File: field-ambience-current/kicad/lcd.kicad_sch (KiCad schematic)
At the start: 5 parts, among them J3 LCD 1.9in ST7789 320x170 SPI-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, Q2 2N7002 (LCD-Backlight Low-Sid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

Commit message: audit: fix J3/J6/J7 LCSC doc-drift; flag H743 firmware cell-read gap (r18.76)
User asked to check for any BOM or device-functionality issues. Ran a
systematic audit:

BOM checks:
- No duplicate reference designators across all 201 placed instances
  (verified against the schematic's actual instance paths, not the
  per-sheet symbol-library templates which share generic single-letter
  placeholder refs by design).
- jlc_bom.csv parses cleanly despite several part descriptions containing
  embedded commas (properly CSV-quoted).
- Generator output verified deterministic across repeated runs.

Found and fixed a real doc<->generator drift: the generator had placeholder
"TBD" text in the LCSC field for J3 (LCD module header) and J6/J7 (speaker
headers), even though BOM_MASTER.md already documented the real, correct
codes for these on-board pin headers (C124383 for J3, C124375 for J6/J7) --
the docs had been updated at some point but the generator itself never was.
Synced the generator to use the already-verified codes; jlc_bom.csv now has
zero remaining placeholder LCSC values except the one legitimate case (J4
Tag-Connect, a genuine vendor-direct part with no LCSC listing, already
audited in BOM_MASTER's r18.37 entry).

Functionality check (found, NOT fixed -- flagging only, this session stays
hardware-only per prior PRs):
- src/hal_h743/main_h743.c (the actual STM32H743 product target) still has
  a commented-out TODO stub describing the retired analog Hall-ADC cell-read
  path (adc_read_norm), which has had no signal source since r18.73 moved
  cells to digital MCP23017 GPIO buttons. If implemented literally as
  written, cells would not function on real hardware.
- src/hal_pico/main_pico.c (the bench target) already has a correct, tested
  implementation: it reads cell presses as MCP23017 GPIO edges directly
  (mirroring the modifier-button code two lines above it in the same main
  loop) and calls engine_note_on/off, bypassing the old velocity state
  machine entirel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
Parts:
- J3: LCSC TBD (Modul, separat bestellen) -> C124383; MPN TBD (LCD-Modul separat: Adafruit 5394-Klasse / ER-TFT019) -> 1x8 2.54mm pin header (the on-board connector; the LCD modu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
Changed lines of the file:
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@@
       (property "Datasheet" "~" (at 140.0 100.0 0)
         (effects (font (size 1.27 1.27)) hide))
-      (property "MPN" "TBD (LCD-Modul separat: Adafruit 5394-Klasse / ER-TFT019)" (at 142.54 103.81 0)
+      (property "MPN" "1x8 2.54mm pin header (the on-board connector; the LCD module itself plugs in separately, off-board, see §C / BOM_MASTER §5)" (at 142.54 103.81 0)
         (effects (font (size 1.27 1.27)) hide))
-      (property "LCSC" "TBD (Modul, separat bestellen)" (at 142.54 105.08 0)
+      (property "LCSC" "C124383" (at 142.54 105.08 0)
         (effects (font (size 1.27 1.27)) hide))
       (property "FP_NOTE" "Standard 2.54mm 1x8-Header (PinHeader_1x08_P2.54mm_Vertical, KiCad-Standard, JEDEC). Adafruit 5394-Pinraster auf 2.54mm — passt 1:1." (at 142.54 106.35 0)

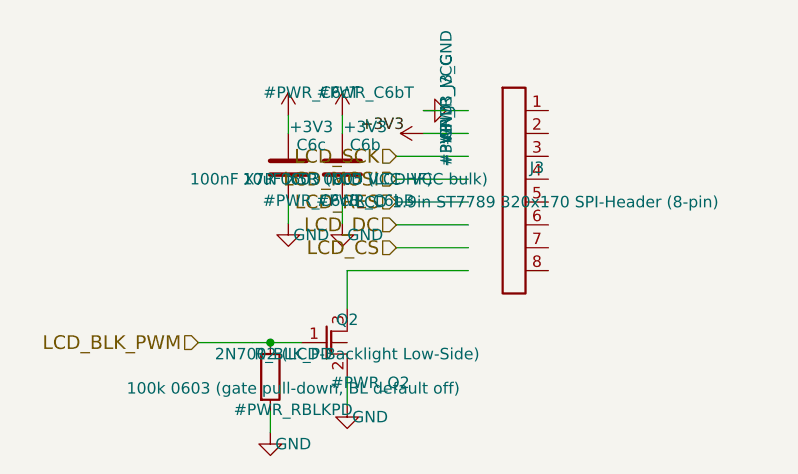
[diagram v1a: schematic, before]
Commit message: fix(pcb): geometric pin-level ERC — 7 copper shorts, 4 open circuits, boost loop instability (r18.80) (#92)
Headless geometric ERC (every pin anchor vs every wire segment, union-find
net build, hier-label/root-pin matching) over all 7 sheets found 12 real
defects; each verified in generator source and fixed there.

Copper shorts (pin/label anchors landing on foreign wires):
- power_tree: USB D+ AND D- hard-shorted to +5V — the U5 LDO block sat in
  the USB data corridor (EN pin on the DP wire, IN pin on the DM wire,
  rail drop overlapping the ESD VBUS wire). Block moved to (130,130).
- mcp: I2C_SCL shorted to GND — C5's GND pin landed exactly on the SCL
  wire (VDD pin 9 and SCL pin 12 are exactly 3 grid rows = 7.62mm apart,
  the cap's pin pitch). Entire I2C bus (U2+U6+U10) was dead. C5/C5b moved.
- audio: PCM_XSMT and I2S_LRCK shorted to GND (same 7.62mm trap, C8a/C8b
  and C_LDOO) — DAC permanently muted / no word clock. Caps flipped up.
- stm32: BOOT0 permanently HIGH twice over (+3V3 flag placed on the BOOT0
  node point; SW_BOOT wire drawn through its own pin-2 anchor) — MCU would
  always enter the ROM bootloader, never firmware.
- stm32: VDDA copper-tied to VDD (pin-21 stub drawn through the VDD pin-100
  anchor), bypassing FB2.
- battery: U8_SW_NODE label sat on the SW/BOOT wire crossing, merging the
  bootstrap net with the switch node (C_BOOT ineffective).

Open circuits:
- lcd: J3 LCD header — all 8 pins floating (wiring assumed KiCad-standard
  pins at -5.08 left; custom lib has pins at +3.81 right). J3 rotated 180.
- stm32: J4 SWD header — all 3 pins floating (same assumption). Board was
  unprogrammable.
- stm32: FB2 rotated 90 off its wires — both pins floating (VDDA had no
  intended supply path).
- stm32: lib_symbols entry lacked the MCU: prefix — KiCad cannot resolve
  U1 at all (exact lib_id match required).

Boost control loop (TPS61089, TI SLVSD38C eqs 15/17/18, validated by
reproducing TI's own 9V/2A reference values):
- R_COMP 22k -> 6.2k (n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
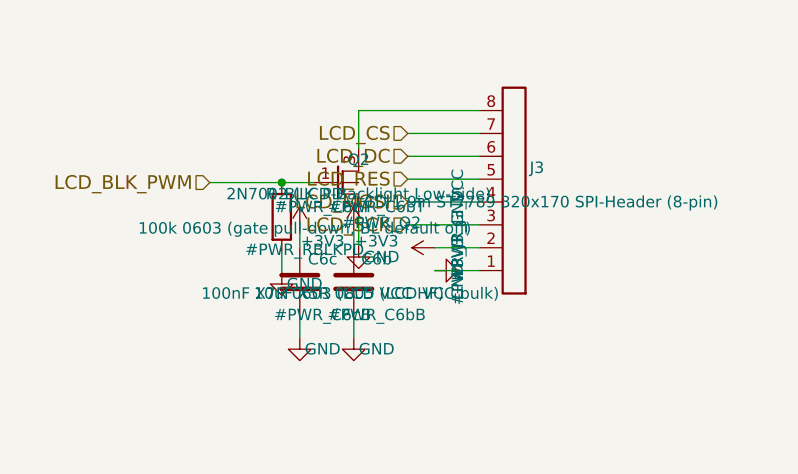
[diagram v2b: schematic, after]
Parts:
- C6b: MPN CL21A106KOQNNNE -> CL21A106KAYNNNE
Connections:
- net +3V3: now also J3.2 (Pin_2)
- net GND: now also J3.1 (Pin_1)
- net LCD_CS: now also J3.7 (Pin_7)
- net LCD_DC: now also J3.6 (Pin_6)
- net LCD_MOSI: now also J3.4 (Pin_4)
- net LCD_RES: now also J3.5 (Pin_5)
- net LCD_SCK: now also J3.3 (Pin_3)
- net at Q2.3 (D): now also J3.8 (Pin_8)
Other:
- moved on the sheet: C6b, C6c, J3, Q2, R_BLK_PD
